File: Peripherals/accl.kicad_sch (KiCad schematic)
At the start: 2 parts, among them U6 ADXL343

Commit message: Reorganised repo
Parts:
- C19: value 470nF -> (none); footprint Capacitor_SMD:C_0603_1608Metric -> (none)
- U6: value ADXL343 -> (none); footprint Package_LGA:LGA-14_3x5mm_P0.8mm_LayoutBorder1x6y -> (none)
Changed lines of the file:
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@@
   (symbol (lib_id "power:+3V3") (at 57.15 25.4 0) (unit 1)
     (in_bom yes) (on_board yes) (fields_autoplaced)
-    (property "Reference" "#PWR041" (id 0) (at 57.15 29.21 0)
+    (property "Reference" "#PWR?" (id 0) (at 57.15 29.21 0)
       (effects (font (size 1.27 1.27)) hide)
     )
-    (property "Value" "+3V3" (id 1) (at 57.15 20.32 0))
+    (property "Value" "" (id 1) (at 57.15 20.32 0))
     (property "Footprint" "" (id 2) (at 57.15 25.4 0)
       (effects (font (size 1.27 1.27)) hide)
@@
     (in_bom yes) (on_board yes) (fields_autoplaced)
     (property "Reference" "U6" (id 0) (at 67.31 39.1412 0))
-    (property "Value" "ADXL343" (id 1) (at 67.31 41.6812 0))
-    (property "Footprint" "Package_LGA:LGA-14_3x5mm_P0.8mm_LayoutBorder1x6y" (id 2) (at 52.07 45.72 0)
+    (property "Value" "" (id 1) (at 67.31 41.6812 0))
+    (property "Footprint" "" (id 2) (at 52.07 45.72 0)
       (effects (font (size 1.27 1.27)) hide)
     )
@@
       (effects (font (size 1.27 1.27)) (justify left))
     )
-    (property "Value" "470nF" (id 1) (at 91.44 36.8362 0)
+    (property "Value" "" (id 1) (at 91.44 36.8362 0)
       (effects (font (size 1.27 1.27)) (justify left))
     )
-    (property "Footprint" "Capacitor_SMD:C_0603_1608Metric" (id 2) (at 88.9 35.56 0)
+    (property "Footprint" "" (id 2) (at 88.9 35.56 0)
       (effects (font (size 1.27 1.27)) hide)
     )
@@
   (symbol (lib_id "power:GND") (at 52.07 63.5 0) (unit 1)
     (in_bom yes) (on_board yes) (fields_autoplaced)
-    (property "Reference" "#PWR040" (id 0) (at 52.07 69.85 0)
+    (property "Reference" "#PWR?" (id 0) (at 52.07 69.85 0)
       (effects (font (size 1.27 1.27)) hide)
     )
-    (property "Value" "GND" (id 1) (at 52.07 68.58 0))
+    (property "Value" "" (id 1) (at 52.07 68.58 0))
     (property "Footprint" "" (id 2) (at 52.07 63.5 0)
       (effects (font (size 1.27 1.27)) hide)
@@
   (symbol (lib_id "power:+3V3") (at 88.9 24.13 0) (unit 1)
     (in_bom yes) (on_board yes) (fields_autoplaced)
-    (property "Reference" "#PWR042" (id 0) (at 88.9 27.94 0)
+    (property "Reference" "#PWR?" (id 0) (at 88.9 27.94 0)
       (effects (font (size 1.27 1.27)) hide)
     )
-    (property "Value" "+3V3" (id 1) (at 88.9 19.05 0))
+    (property "Value" "" (id 1) (at 88.9 19.05 0))
     (property "Footprint" "" (id 2) (at 88.9 24.13 0)
       (effects (font (size 1.27 1.27)) hide)
@@
   (symbol (lib_id "power:GND") (at 88.9 46.99 0) (unit 1)
     (in_bom yes) (on_board yes) (fields_autoplaced)
-    (property "Reference" "#PWR043" (id 0) (at 88.9 53.34 0)
+    (property "Reference" "#PWR?" (id 0) (at 88.9 53.34 0)
       (effects (font (size 1.27 1.27)) hide)
     )
-    (property "Value" "GND" (id 1) (at 88.9 52.07 0))
+    (property "Value" "" (id 1) (at 88.9 52.07 0))
     (property "Footprint" "" (id 2) (at 88.9 46.99 0)
       (effects (font (size 1.27 1.27)) hide)

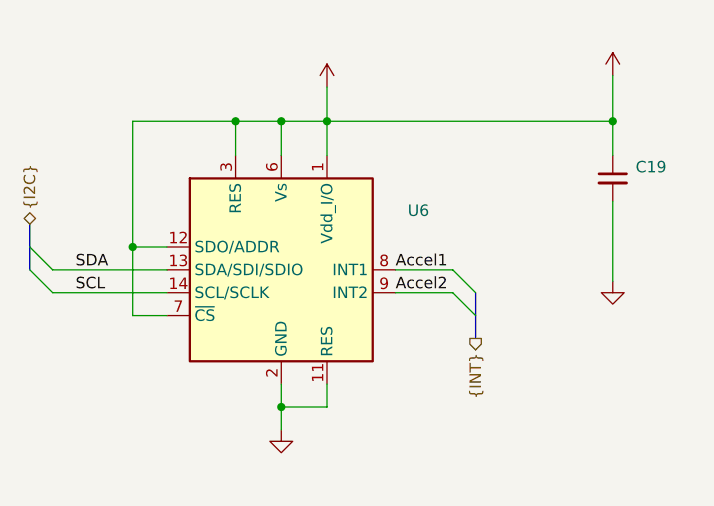
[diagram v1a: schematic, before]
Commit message: rev2 changes excluding pyro
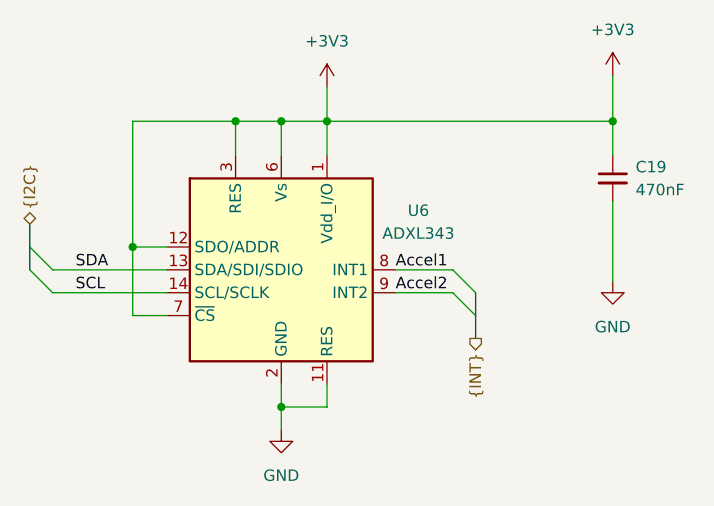
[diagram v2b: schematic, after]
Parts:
- C19: value (none) -> 470nF; footprint (none) -> Capacitor_SMD:C_0603_1608Metric
- U6: value (none) -> ADXL343; footprint (none) -> Package_LGA:LGA-14_3x5mm_P0.8mm_LayoutBorder1x6y
